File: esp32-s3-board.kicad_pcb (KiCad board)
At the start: 2 copper layers, 65 x 45 mm, 60 parts, among them J1 USB_C_Receptacle_USB2.0_14P, J2 OV2640, J3 Micro_SD_Card, J4 Conn_01x08, U1 ESP32-S3, U2 MCP1700x-280xxTT, U3 W25Q128JVS, U4 ESP-PSRAM64H, U6 NCP1117-1.5_SOT223, U7 MCP1700x-330xxTT, Y1 40MHz

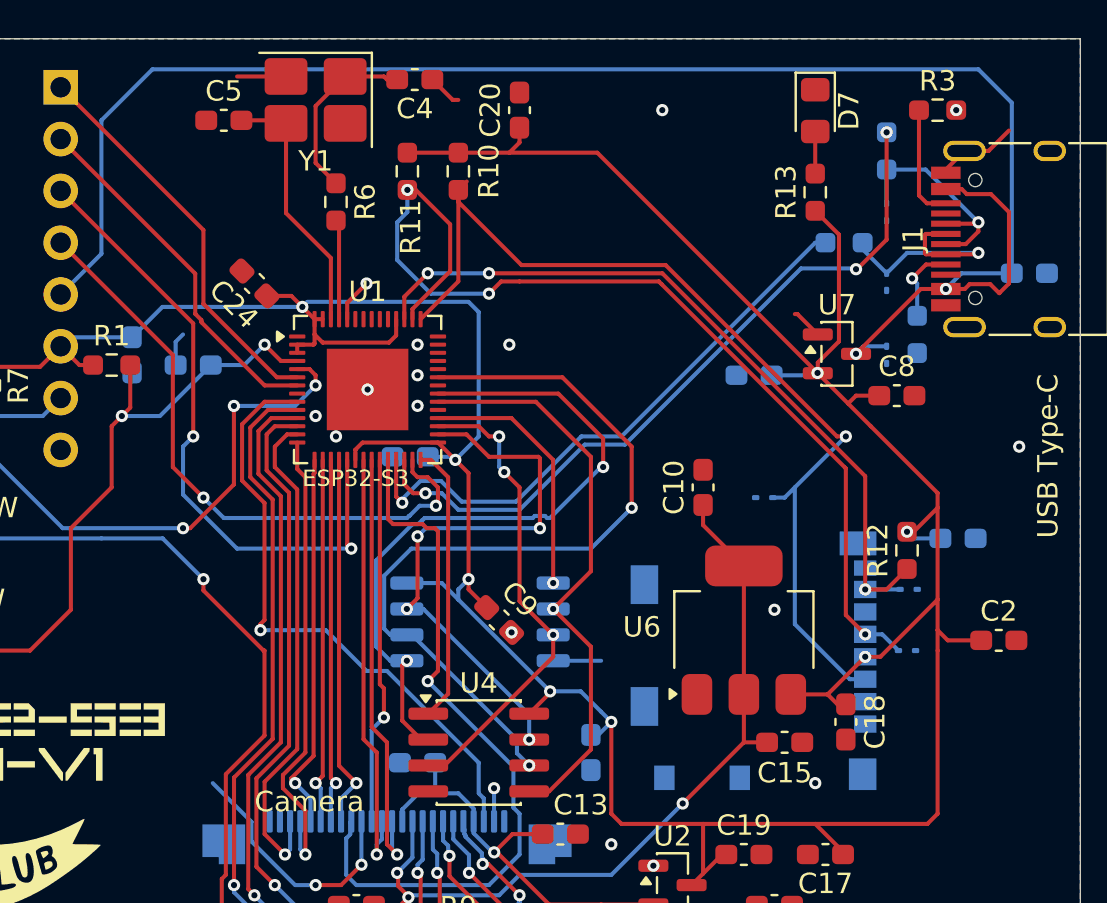
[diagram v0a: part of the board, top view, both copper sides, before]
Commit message: Fixed README.md and fabrication files
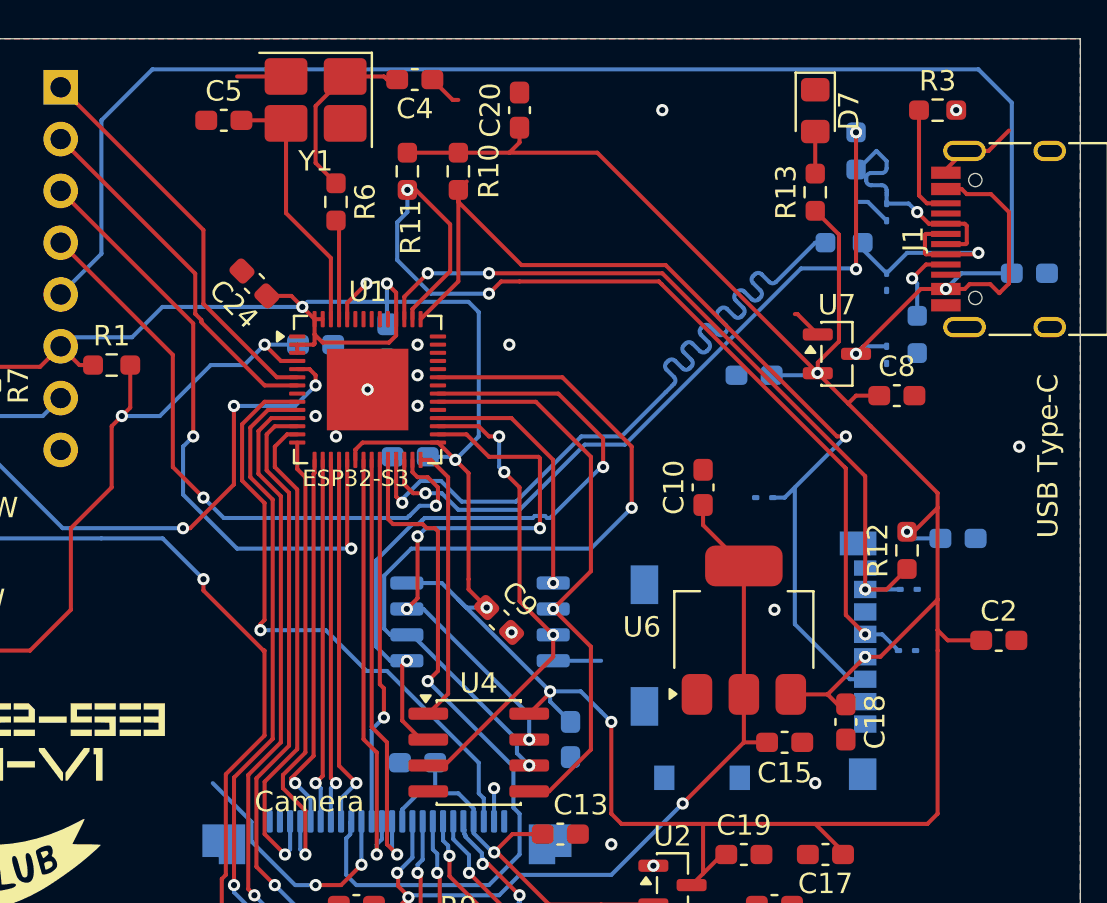
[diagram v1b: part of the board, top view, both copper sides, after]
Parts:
- moved C22 12.5 mm to (146.0, 69.9)
- moved C3 6.08 mm to (142.5, 70.0), turned to 0 degrees
- moved R5 1.50 mm to (169.0, 60.5)
- moved C7 1.19 mm to (155.0, 89.4)
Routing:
- net Net-(U1-GPIO19/USB_D-): track 29.2 -> 38.5 mm
- net +3V3: track 185.0 -> 190.0 mm, vias 8 -> 9
- net Net-(U1-CHIP_PU): track 28.3 -> 30.0 mm
- net D+: track 11.2 -> 12.2 mm
- net Net-(U1-GPIO20/USB_D+): track 36.1 -> 35.5 mm
